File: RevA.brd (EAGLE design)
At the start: 106 x 48 mm, 57 parts, among them IC1 MAX31855, IC10 DS3231/SO, IC3 MAX31855, IC4 MAX31855, IC5 MAX31855, IC9 ATMEGA32U4-AU, J1 1X2-3.5MM, J2 1X2-3.5MM, J3 1X2-3.5MM, J4 1X2-3.5MM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

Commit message: Changes after review
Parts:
- added C10, C11, C12, C20: 1uF, microbuilder:0603-NO
- added TP1: TPPAD1-13, testpad:P1-13
- moved X1 103.6 mm to (101.9, 11.9), turned to 270 degrees
- moved B1 95.1 mm to (168.6, 8.70)
- moved C7 85.6 mm to (79.0, -9.00)
- moved C18 84.2 mm to (61.5, -13.8)
- moved R14 75.5 mm to (47.2, 5.15), turned to 270 degrees
- moved ISP1 75.4 mm to (151.5, 41.2)
- moved C16 73.8 mm to (98.5, 28.2), turned to 0 degrees
- moved R12 72.8 mm to (63.2, 6.98)
- moved L1 66.6 mm to (48.8, 13.2)
- moved IC9 60.6 mm to (87.8, 25.5), turned to 270 degrees
- moved X3 57.2 mm to (88.9, 43.7), turned to 180 degrees
- moved R15 56.1 mm to (90.5, 39.0)
- moved R13 55.0 mm to (47.4, 23.2)
- moved R16 53.7 mm to (88.2, 39.0)
- moved C13 52.0 mm to (32.8, 20.9)
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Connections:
- removed net 11: IC9.12
- removed net 2: IC9.19
- removed net 3: IC9.18
- removed net 3.3V: C19.2, IC10.2, R18.1, R19.1
- net +3V3: now also C10.1, C11.1, C12.1, C19.2, C20.1, IC10.2, R18.1, R19.1
- net GND: now also C10.2, C11.2, C12.2, C20.2
- net SCL: now also IC9.18
- net SDA: now also IC9.19
- net SD_CS: now also IC9.12, TP1.TP; no longer IC9.25
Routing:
- net +3V3: track 190.9 -> 13.8 mm, vias 6 -> 0
- net MISO: track 130.4 -> 0.00 mm, vias 4 -> 0
- net MOSI: track 112.2 -> 0.00 mm, vias 2 -> 0
- net SCK: track 153.8 -> 43.4 mm, vias 8 -> 4
- net VBUS: track 91.8 -> 14.2 mm
- net VBAT: track 65.1 -> 0.00 mm, vias 3 -> 0
- net RST: track 54.7 -> 0.00 mm
- net D-: track 43.5 -> 0.00 mm, vias 2 -> 0
- net SD_CS: track 43.4 -> 0.00 mm, vias 2 -> 0
- net D+: track 42.9 -> 0.00 mm, vias 2 -> 0
- net N$31: track 16.5 -> 0.00 mm
- net 8: track 16.1 -> 0.00 mm
- net 9: track 14.4 -> 0.00 mm
- net N$26: track 10.3 -> 0.00 mm
- net SDA: track 10.2 -> 0.00 mm
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
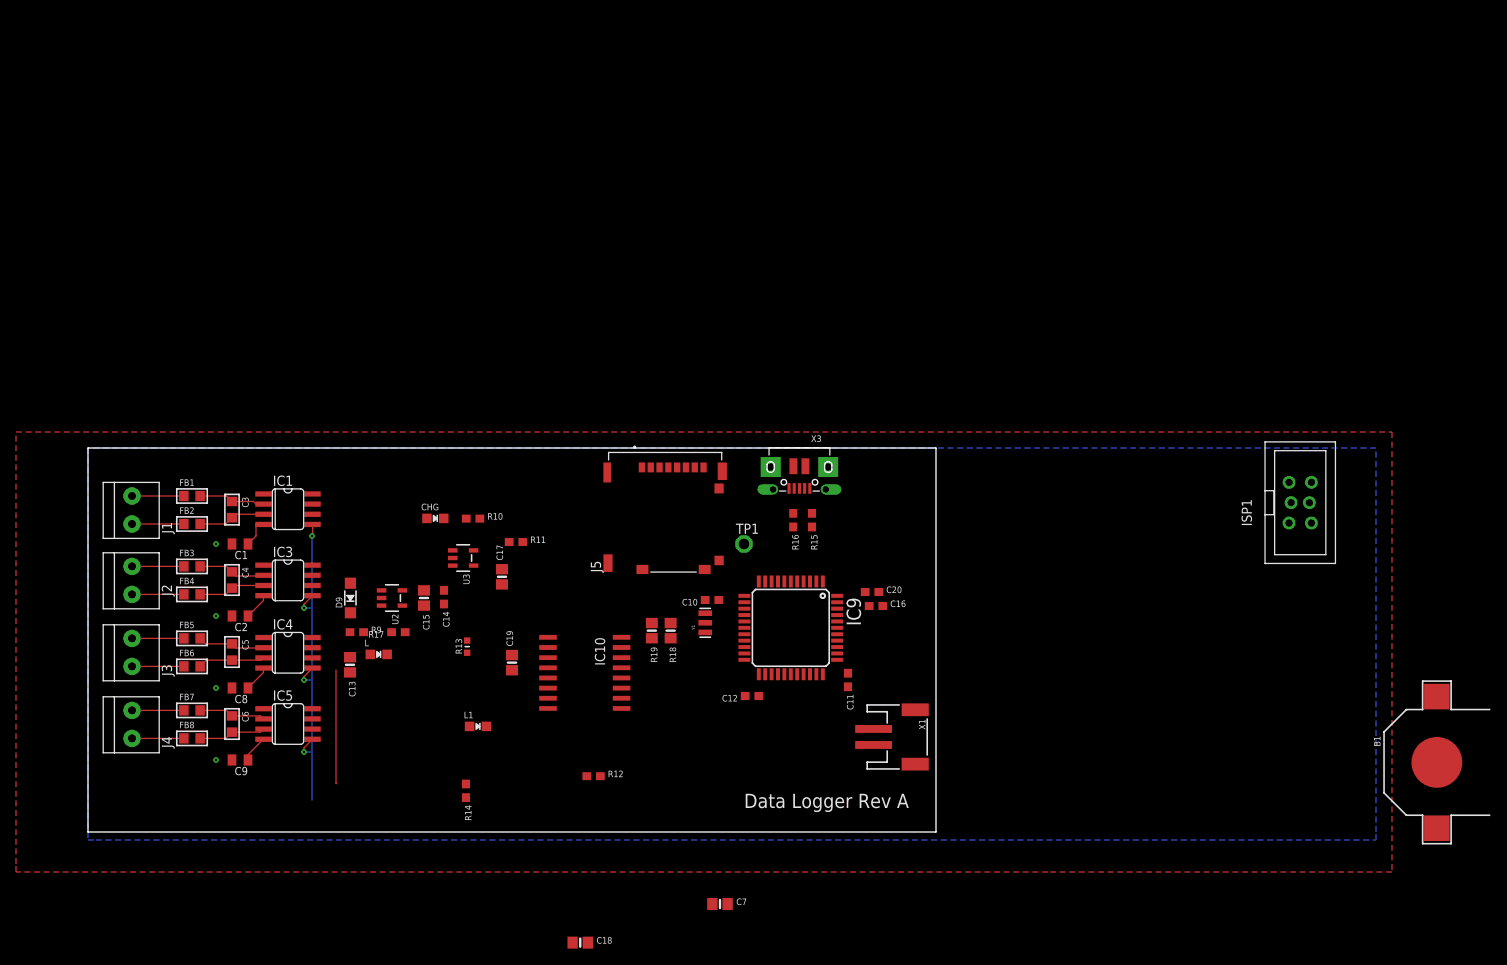
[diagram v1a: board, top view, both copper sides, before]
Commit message: Added new layout scheme
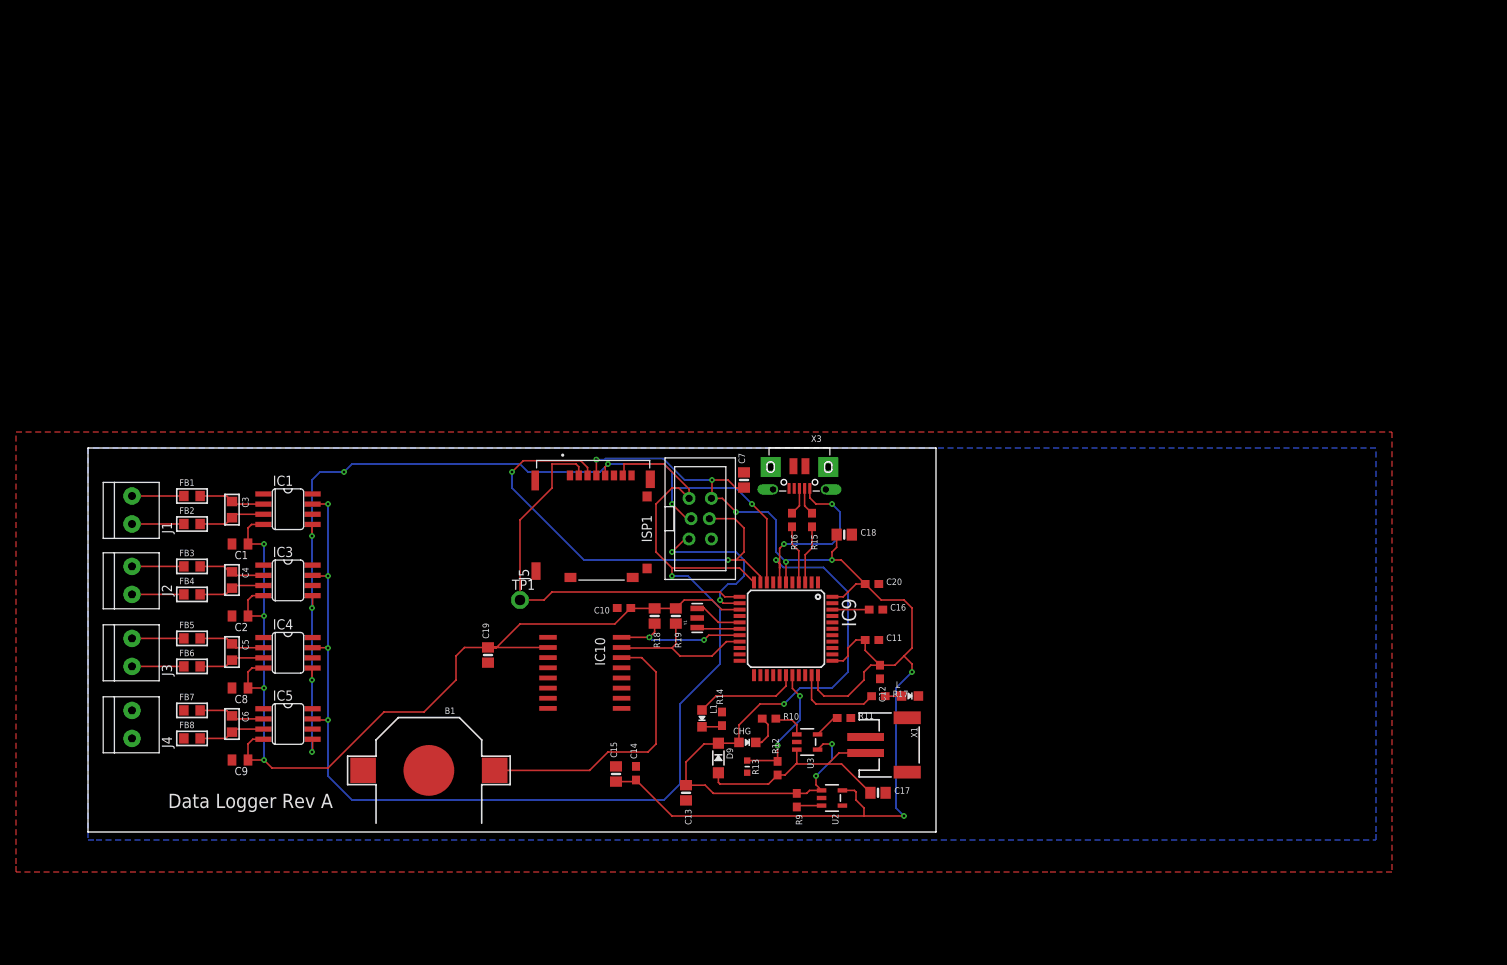
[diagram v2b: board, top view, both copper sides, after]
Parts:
- moved B1 126.0 mm to (42.6, 7.70), turned to 180 degrees
- moved ISP1 75.0 mm to (76.5, 39.2)
- moved L 66.6 mm to (102.8, 17.0)
- moved C18 60.7 mm to (94.5, 37.2)
- moved R17 60.5 mm to (98.8, 17.0), turned to 0 degrees
- moved U2 60.4 mm to (93.0, 4.25)
- moved R9 58.9 mm to (88.6, 3.98), turned to 270 degrees
- moved C17 54.2 mm to (98.8, 4.90), turned to 0 degrees
- moved C7 53.1 mm to (82.0, 44.0), turned to 90 degrees
- moved D9 50.2 mm to (78.8, 9.25), turned to 270 degrees
- moved U3 48.8 mm to (89.9, 11.2)
- moved CHG 48.0 mm to (82.4, 11.2)
- moved R11 46.5 mm to (94.5, 14.2)
- moved C13 44.9 mm to (74.8, 4.90)
- moved R10 44.7 mm to (85.1, 14.2)
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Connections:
- removed net DO: IC1.7, IC3.7, IC4.7, IC5.7
- net MISO: now also IC1.7, IC3.7, IC4.7, IC5.7
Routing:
- net +3V3: track 13.8 -> 295.7 mm, vias 0 -> 11
- net MISO: track 0.00 -> 158.0 mm, vias 0 -> 5
- net VBUS: track 14.2 -> 98.6 mm, vias 0 -> 6
- net SCK: track 43.4 -> 117.4 mm, vias 4 -> 8
- net VBAT: track 0.00 -> 65.5 mm
- net MOSI: track 0.00 -> 59.0 mm, vias 0 -> 2
- net SD_CS: track 0.00 -> 51.3 mm
- net RST: track 0.00 -> 21.7 mm, vias 0 -> 2
- net SDA: track 0.00 -> 19.2 mm
- net SCL: track 0.00 -> 17.1 mm, vias 0 -> 2
- net 9: track 0.00 -> 16.2 mm, vias 0 -> 2
- net 8: track 0.00 -> 13.1 mm
- net 13: track 0.00 -> 11.2 mm
- net D+: track 0.00 -> 7.51 mm
- net D-: track 0.00 -> 7.30 mm
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
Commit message: Finalized layout and added libraries
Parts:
- moved FB4 5.00 mm to (13.0, 34.7)
- moved IC3 5.00 mm to (25.0, 36.5)
- moved R10 5.00 mm to (85.1, 19.2)
- moved C1 5.00 mm to (19.0, 41.0)
- moved C10 5.00 mm to (67.0, 33.0)
- moved C11 5.00 mm to (98.0, 29.0)
- moved C12 5.00 mm to (99.0, 25.0)
- moved C13 5.00 mm to (74.8, 9.90)
- moved C14 5.00 mm to (68.5, 12.3)
- moved C15 5.00 mm to (66.0, 12.2)
- moved C17 5.00 mm to (98.8, 9.90)
- moved C18 5.00 mm to (94.5, 42.2)
- moved C19 5.00 mm to (50.0, 27.1)
- moved C2 5.00 mm to (19.0, 32.0)
- moved C20 5.00 mm to (98.0, 36.0)
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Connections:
- removed net 0: IC9.20
- removed net 1: IC9.21
- net CS-1: now also IC9.20
- net CS-2: now also IC9.21
- net CS-3: now also IC9.22
- net CS-4: now also IC9.25
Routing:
- net CS-4: track 0.00 -> 87.4 mm, vias 0 -> 2
- net +3V3: track 295.7 -> 377.8 mm, vias 11 -> 12
- net CS-2: track 0.00 -> 65.7 mm, vias 0 -> 2
- net CS-3: track 0.00 -> 64.7 mm, vias 0 -> 2
- net CS-1: track 0.00 -> 63.1 mm, vias 0 -> 2
- net N$15: track 0.00 -> 6.48 mm
- net N$13: track 0.00 -> 6.48 mm
- net MOSI: track 59.0 -> 61.9 mm
- net SDA: track 19.2 -> 19.8 mm, vias 0 -> 2
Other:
- board size 106 x 48 mm -> 106 x 53 mm
- board text added: "Colossus Rev A Khan, A. 08.15.18"
- board text removed: "Data Logger Rev A"

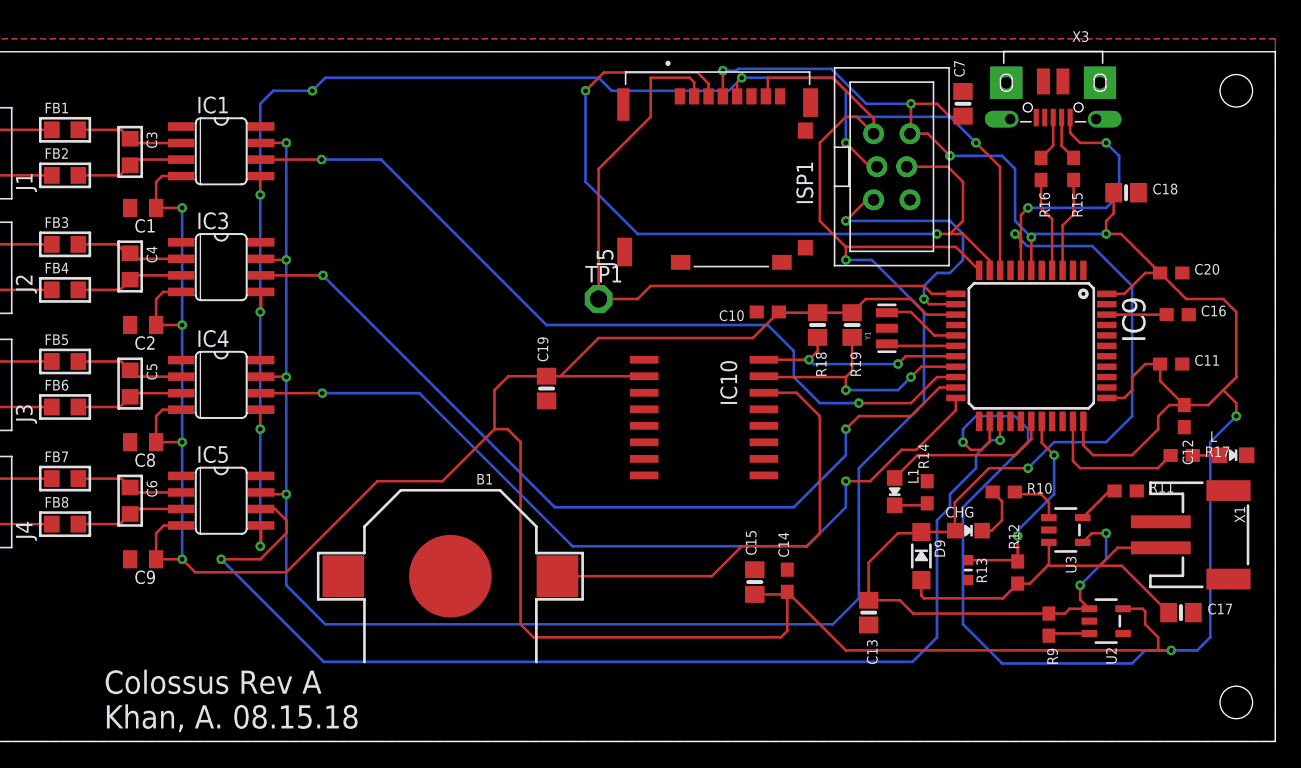
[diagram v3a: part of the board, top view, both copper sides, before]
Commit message: Increased power track widths
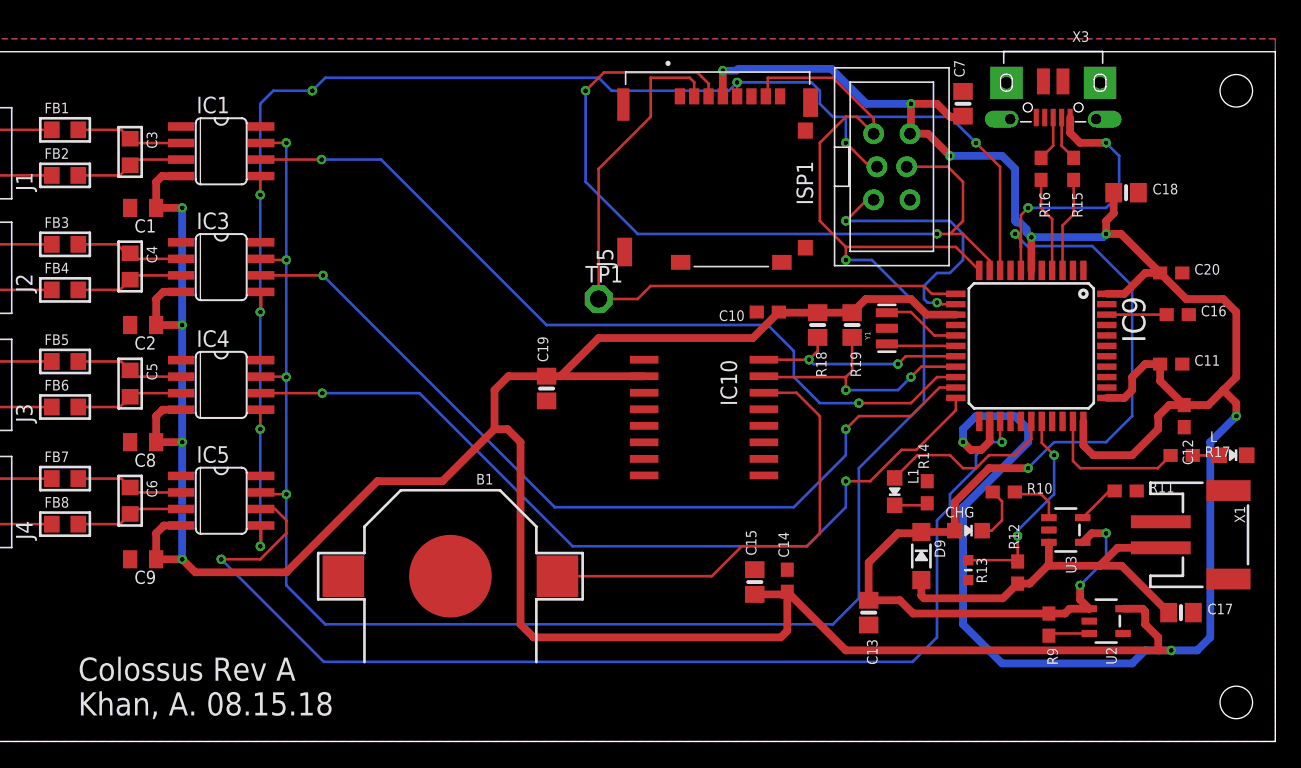
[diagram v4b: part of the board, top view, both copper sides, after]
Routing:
- net SCK: track 117.4 -> 116.0 mm
- net 8: track 13.1 -> 13.9 mm
- net CS-4: track 87.4 -> 87.9 mm
